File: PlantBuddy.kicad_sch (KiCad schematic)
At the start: 75 parts, among them J1 USB_C_Receptacle_USB2.0, J101 JST, J102 Debug, J4 External, SW1 SW_Push, U1 LTR-303ALS-01, U101 AP2139AK-3.0TRG1, U102 nRF52832-QFAA, U104 XB5350A, U105 CN809T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

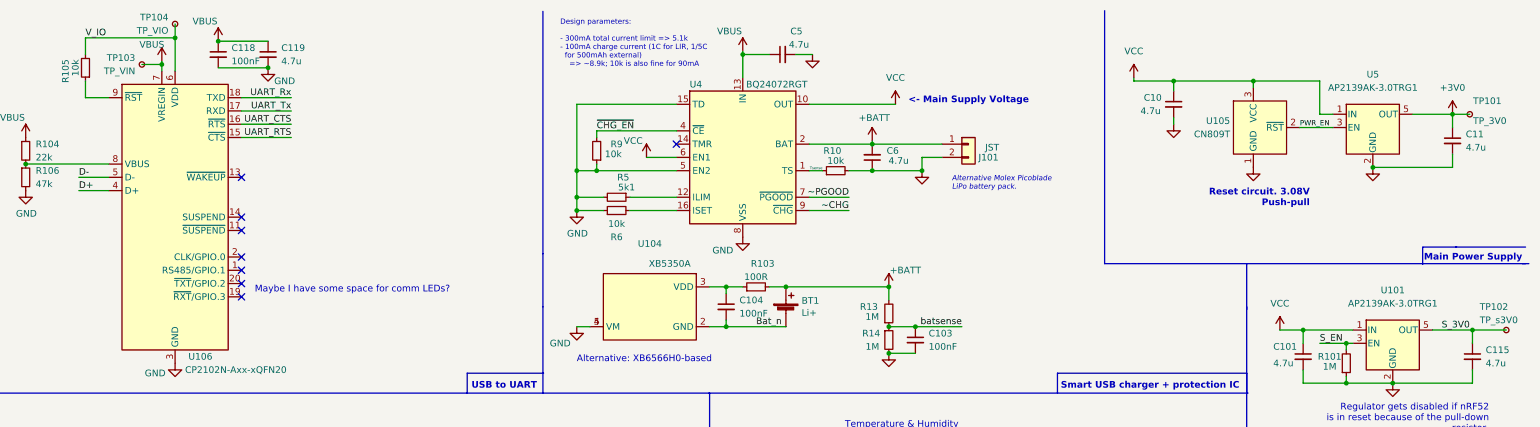
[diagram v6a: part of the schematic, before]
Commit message: Changed antenna to 1.6mm-compatible one
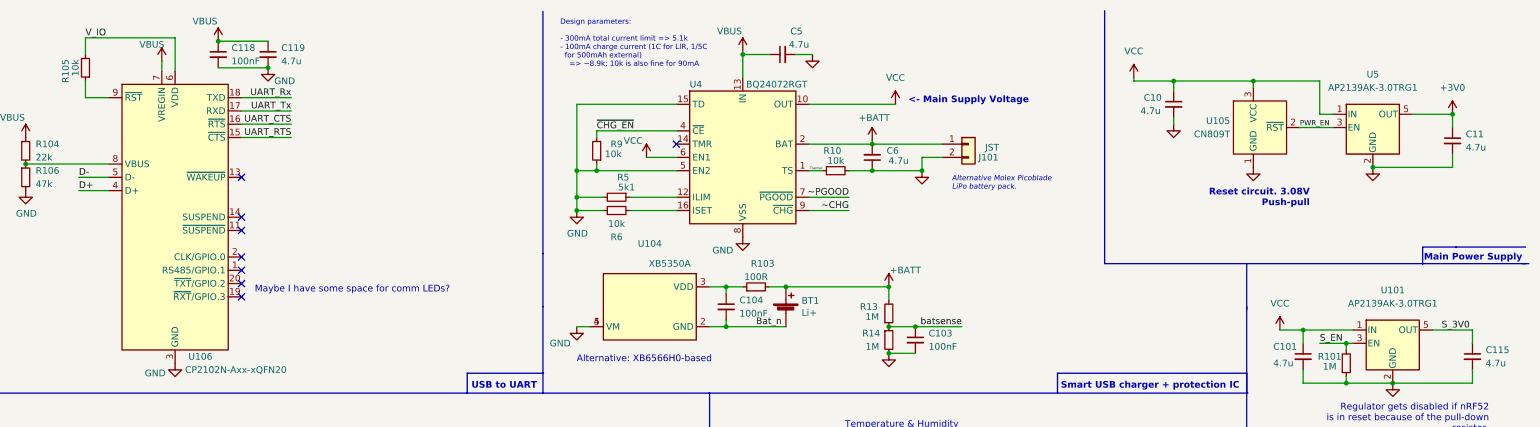
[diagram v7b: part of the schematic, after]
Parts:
- removed TP101: TP_3V0, TestPoint:TestPoint_Pad_D1.0mm, symbol Connector:TestPoint_Small
- removed TP102: TP_s3V0, TestPoint:TestPoint_Pad_D1.0mm, symbol Connector:TestPoint_Small
- removed TP103: TP_VIN, TestPoint:TestPoint_Pad_D1.0mm, symbol Connector:TestPoint_Small
- removed TP104: TP_VIO, TestPoint:TestPoint_Pad_D1.0mm, symbol Connector:TestPoint_Small
- AE101: footprint RF_Antenna:Texas_SWRA117D_2.4GHz_Left -> wch-antenna:ANT-F-1-2.4G-1.6MM-FR4-WCH
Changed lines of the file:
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@@
     (comment 2 "Version 2: Changed to an ESP32-C3 based project due to chip shortage.")
   )
-  (junction (at 398.018 73.025) (diameter 0) (color 0 0 0 0)
-  )
   (junction (at 226.695 47.625) (diameter 0) (color 0 0 0 0)
   )
@@
   (junction (at 167.64 22.86) (diameter 0) (color 0 0 0 0)
   )
-  (junction (at 147.32 22.225) (diameter 0) (color 0 0 0 0)
-  )
   (junction (at 373.888 75.565) (diameter 0) (color 0 0 0 0)
   )
@@
   (junction (at 137.16 147.32) (diameter 0) (color 0 0 0 0)
   )
-  (junction (at 149.86 17.145) (diameter 0) (color 0 0 0 0)
-  )
   (junction (at 266.7 64.77) (diameter 0) (color 0 0 0 0)
   )
@@
     (stroke (width 0) (type default) (color 0 0 0 0))
   )
-  (wire (pts (xy 149.86 14.478) (xy 149.86 17.145))
-    (stroke (width 0) (type default) (color 0 0 0 0))
-  )
   (wire (pts (xy 149.86 125.095) (xy 149.86 126.365))
     (stroke (width 0) (type default) (color 0 0 0 0))
@@
     (stroke (width 0) (type default) (color 0 0 0 0))
   )
-  (wire (pts (xy 147.32 22.225) (xy 147.32 23.495))
+  (wire (pts (xy 147.32 21.59) (xy 147.32 23.495))
     (stroke (width 0) (type default) (color 0 0 0 0))
   )
@@
     (stroke (width 0) (type default) (color 0 0 0 0))
   )
-  (wire (pts (xy 394.208 31.75) (xy 397.51 31.75))
-    (stroke (width 0) (type default) (color 0 0 0 0))
-  )
   (wire (pts (xy 133.35 191.135) (xy 127.635 191.135))
     (stroke (width 0) (type default) (color 0 0 0 0))
@@
     (stroke (width 0) (type default) (color 0 0 0 0))
   )
-  (wire (pts (xy 398.018 73.025) (xy 404.495 73.025))
-    (stroke (width 0) (type default) (color 0 0 0 0))
-  )
   (wire (pts (xy 258.445 20.32) (xy 263.525 20.32))
     (stroke (width 0) (type default) (color 0 0 0 0))
@@
     (stroke (width 0) (type default) (color 0 0 0 0))
   )
-  (wire (pts (xy 143.51 22.225) (xy 147.32 22.225))
-    (stroke (width 0) (type default) (color 0 0 0 0))
-  )
   (wire (pts (xy 43.815 35.56) (xy 43.815 36.83))
     (stroke (width 0) (type default) (color 0 0 0 0))
@@
     (stroke (width 0) (type default) (color 0 0 0 0))
   )
-  (wire (pts (xy 147.32 22.225) (xy 147.32 21.59))
-    (stroke (width 0) (type default) (color 0 0 0 0))
-  )
   (wire (pts (xy 126.365 153.67) (xy 126.365 154.94))
     (stroke (width 0) (type default) (color 0 0 0 0))
@@
     (pin "3")
   )
-  (symbol (lib_id "Connector:TestPoint_Small") (at 397.51 31.75 0) (unit 1)
-    (in_bom yes) (on_board yes)
-    (property "Reference" "TP101" (id 0) (at 398.145 29.21 0)
-      (effects (font (size 1.27 1.27)) (justify left))
-    )
-    (property "Value" "TP_3V0" (id 1) (at 398.145 33.02 0)
-      (effects (font (size 1.27 1.27)) (justify left))
-    )
-    (property "Footprint" "TestPoint:TestPoint_Pad_D1.0mm" (id 2) (at 402.59 31.75 0)
-      (effects (font (size 1.27 1.27)) hide)
-    )
-    (property "Datasheet" "~" (id 3) (at 402.59 31.75 0)
-      (effects (font (size 1.27 1.27)) hide)
-    )
-    (pin "1")
-  )
   (symbol (lib_id "PlantBuddy-rescue:GND-power") (at 51.435 29.21 0) (mirror y) (unit 1)
     (in_bom yes) (on_board yes)
@@
       (effects (font (size 1.27 1.27)) (justify left))
     )
-    (property "Footprint" "RF_Antenna:Texas_SWRA117D_2.4GHz_Left" (id 2) (at 40.005 173.99 0)
+    (property "Footprint" "wch-antenna:ANT-F-1-2.4G-1.6MM-FR4-WCH" (id 2) (at 40.005 173.99 0)
       (effects (font (size 1.27 1.27)) hide)
     )
@@
     (pin "2")
   )
-  (symbol (lib_id "Connector:TestPoint_Small") (at 149.86 14.478 0) (mirror x) (unit 1)
-    (in_bom yes) (on_board yes) (fields_autoplaced)
-    (property "Reference" "TP104" (id 0) (at 148.59 13.2079 0)
-      (effects (font (size 1.27 1.27)) (justify right))
-    )
-    (property "Value" "TP_VIO" (id 1) (at 148.59 15.7479 0)
-      (effects (font (size 1.27 1.27)) (justify right))
-    )
-    (property "Footprint" "TestPoint:TestPoint_Pad_D1.0mm" (id 2) (at 154.94 14.478 0)
-      (effects (font (size 1.27 1.27)) hide)
-    )
-    (property "Datasheet" "~" (id 3) (at 154.94 14.478 0)
-      (effects (font (size 1.27 1.27)) hide)
-    )
-    (pin "1")
-  )
   (symbol (lib_id "Device:C_Small") (at 340.868 29.845 0) (unit 1)
     (in_bom yes) (on_board yes)
@@
     (pin "2")
   )
-  (symbol (lib_id "Connector:TestPoint_Small") (at 143.51 22.225 0) (mirror x) (unit 1)
-    (in_bom yes) (on_board yes) (fields_autoplaced)
-    (property "Reference" "TP103" (id 0) (at 142.24 20.9549 0)
-      (effects (font (size 1.27 1.27)) (justify right))
-    )
-    (property "Value" "TP_VIN" (id 1) (at 142.24 23.4949 0)
-      (effects (font (size 1.27 1.27)) (justify right))
-    )
-    (property "Footprint" "TestPoint:TestPoint_Pad_D1.0mm" (id 2) (at 148.59 22.225 0)
-      (effects (font (size 1.27 1.27)) hide)
-    )
-    (property "Datasheet" "~" (id 3) (at 148.59 22.225 0)
-      (effects (font (size 1.27 1.27)) hide)
-    )
-    (pin "1")
-  )
   (symbol (lib_id "Device:C_Small") (at 255.27 68.58 0) (unit 1)
     (in_bom yes) (on_board yes) (fields_autoplaced)
@@
   (symbol (lib_id "PlantBuddy-rescue:GND-power") (at 34.925 180.975 0) (unit 1)
     (in_bom yes) (on_board yes)
-    (property "Reference" "#PWR?" (id 0) (at 34.925 187.325 0)
+    (property "Reference" "#PWR0125" (id 0) (at 34.925 187.325 0)
       (effects (font (size 1.27 1.27)) hide)
     )
@@
     (pin "2")
   )
-  (symbol (lib_id "Connector:TestPoint_Small") (at 404.495 73.025 0) (unit 1)
-    (in_bom yes) (on_board yes)
-    (property "Reference" "TP102" (id 0) (at 399.415 68.58 0)
-      (effects (font (size 1.27 1.27)) (justify left))
-    )
-    (property "Value" "TP_s3V0" (id 1) (at 399.415 71.12 0)
-      (effects (font (size 1.27 1.27)) (justify left))
-    )
-    (property "Footprint" "TestPoint:TestPoint_Pad_D1.0mm" (id 2) (at 409.575 73.025 0)
-      (effects (font (size 1.27 1.27)) hide)
-    )
-    (property "Datasheet" "~" (id 3) (at 409.575 73.025 0)
-      (effects (font (size 1.27 1.27)) hide)
-    )
-    (pin "1")
-  )
   (symbol (lib_id "Regulator_Linear:TLV70235_SOT23-5") (at 382.778 75.565 0) (unit 1)
     (in_bom yes) (on_board yes) (fields_autoplaced)
@@
       (reference "#PWR0124") (unit 1) (value "GND") (footprint "")
     )
+    (path "/a80f6003-26ac-4b9c-a6ac-c9d4176d44bc"
+      (reference "#PWR0125") (unit 1) (value "GND") (footprint "")
+    )
     (path "/586d2ebf-6319-4117-87fd-e9c22eefe240"
       (reference "#PWR0126") (unit 1) (value "GND") (footprint "")
@@
       (reference "#PWR0135") (unit 1) (value "GND") (footprint "")
     )
-    (path "/a80f6003-26ac-4b9c-a6ac-c9d4176d44bc"
-      (reference "#PWR?") (unit 1) (value "GND") (footprint "")
-    )
     (path "/400ec827-23d4-4dc8-9011-0b8d912989c5"
-      (reference "AE101") (unit 1) (value "Antenna_MIFA") (footprint "RF_Antenna:Texas_SWRA117D_2.4GHz_Left")
+      (reference "AE101") (unit 1) (value "Antenna_MIFA") (footprint "wch-antenna:ANT-F-1-2.4G-1.6MM-FR4-WCH")
     )
     (path "/00000000-0000-0000-0000-00005fc5077f"
@@
       (reference "SW1") (unit 1) (value "SW_Push") (footprint "Button_Switch_SMD:Panasonic_EVQPUK_EVQPUB")
     )
-    (path "/1c26dc60-5cd9-46dd-a056-2540f6e81041"
-      (reference "TP101") (unit 1) (value "TP_3V0") (footprint "TestPoint:TestPoint_Pad_D1.0mm")
-    )
-    (path "/ecf6cdec-2b73-4965-a7ee-d33a2a856670"
-      (reference "TP102") (unit 1) (value "TP_s3V0") (footprint "TestPoint:TestPoint_Pad_D1.0mm")
-    )
-    (path "/7bd6b060-e15b-454c-8af7-deb0e6677ade"
-      (reference "TP103") (unit 1) (value "TP_VIN") (footprint "TestPoint:TestPoint_Pad_D1.0mm")
-    )
-    (path "/6f060714-01d1-435f-ae77-dcd77ff91135"
-      (reference "TP104") (unit 1) (value "TP_VIO") (footprint "TestPoint:TestPoint_Pad_D1.0mm")
-    )
     (path "/00000000-0000-0000-0000-0000611aa492"

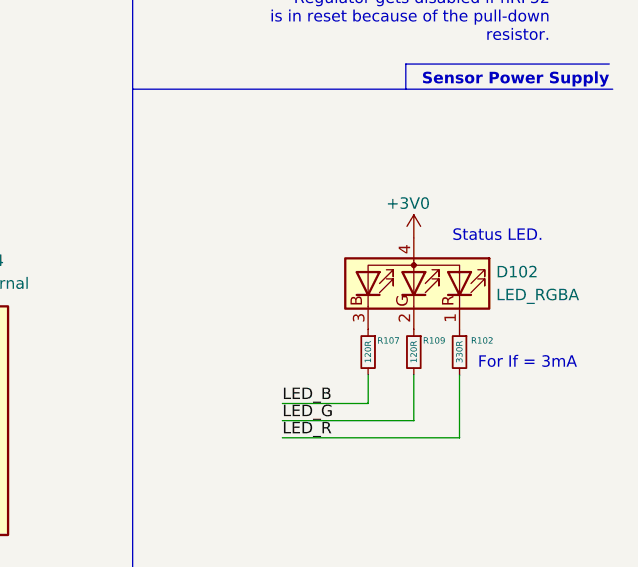
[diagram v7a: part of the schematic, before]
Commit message: Corrected LED pins
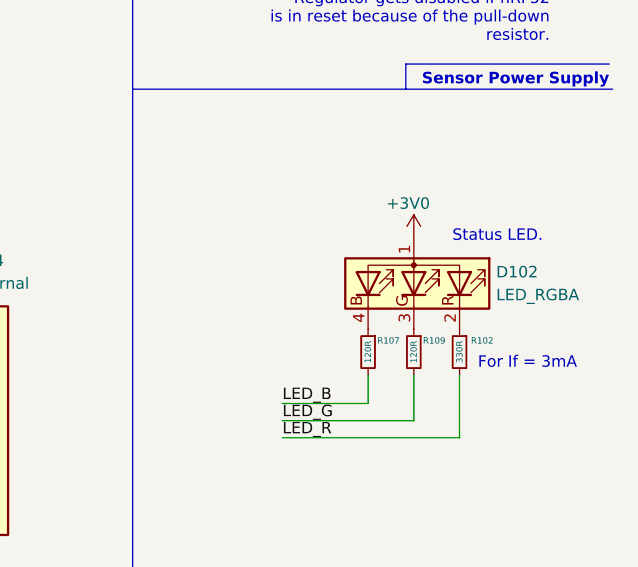
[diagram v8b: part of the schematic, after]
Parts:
- D102: symbol Device:LED_RGBA -> Device:LED_ARGB
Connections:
- net +3V0: now also D102.1 (A); no longer D102.4 (A)
- net at R102.1: now also D102.2 (RK); no longer D102.1 (RK)
- net at R107.1: now also D102.4 (BK); no longer D102.3 (BK)
- net at R109.1: now also D102.3 (GK); no longer D102.2 (GK)
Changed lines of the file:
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@@
     (pin "9")
   )
-  (symbol (lib_id "Device:LED_RGBA") (at 386.08 119.38 270) (mirror x) (unit 1)
+  (symbol (lib_id "Device:LED_ARGB") (at 386.08 119.38 270) (mirror x) (unit 1)
     (in_bom yes) (on_board yes) (fields_autoplaced)
     (property "Reference" "D102" (id 0) (at 395.224 118.1099 90)
